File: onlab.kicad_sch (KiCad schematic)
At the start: 57 parts, among them J1 Battery, J2 HC_SR04, J3 HC_SR04, J4 HC_SR04, J5 DC-Motor, J6 DC-Motor, J7 DC-Motor, SW1 SW_SPDT, SW2 SW_SPDT, SW3 SW_DIP_x03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

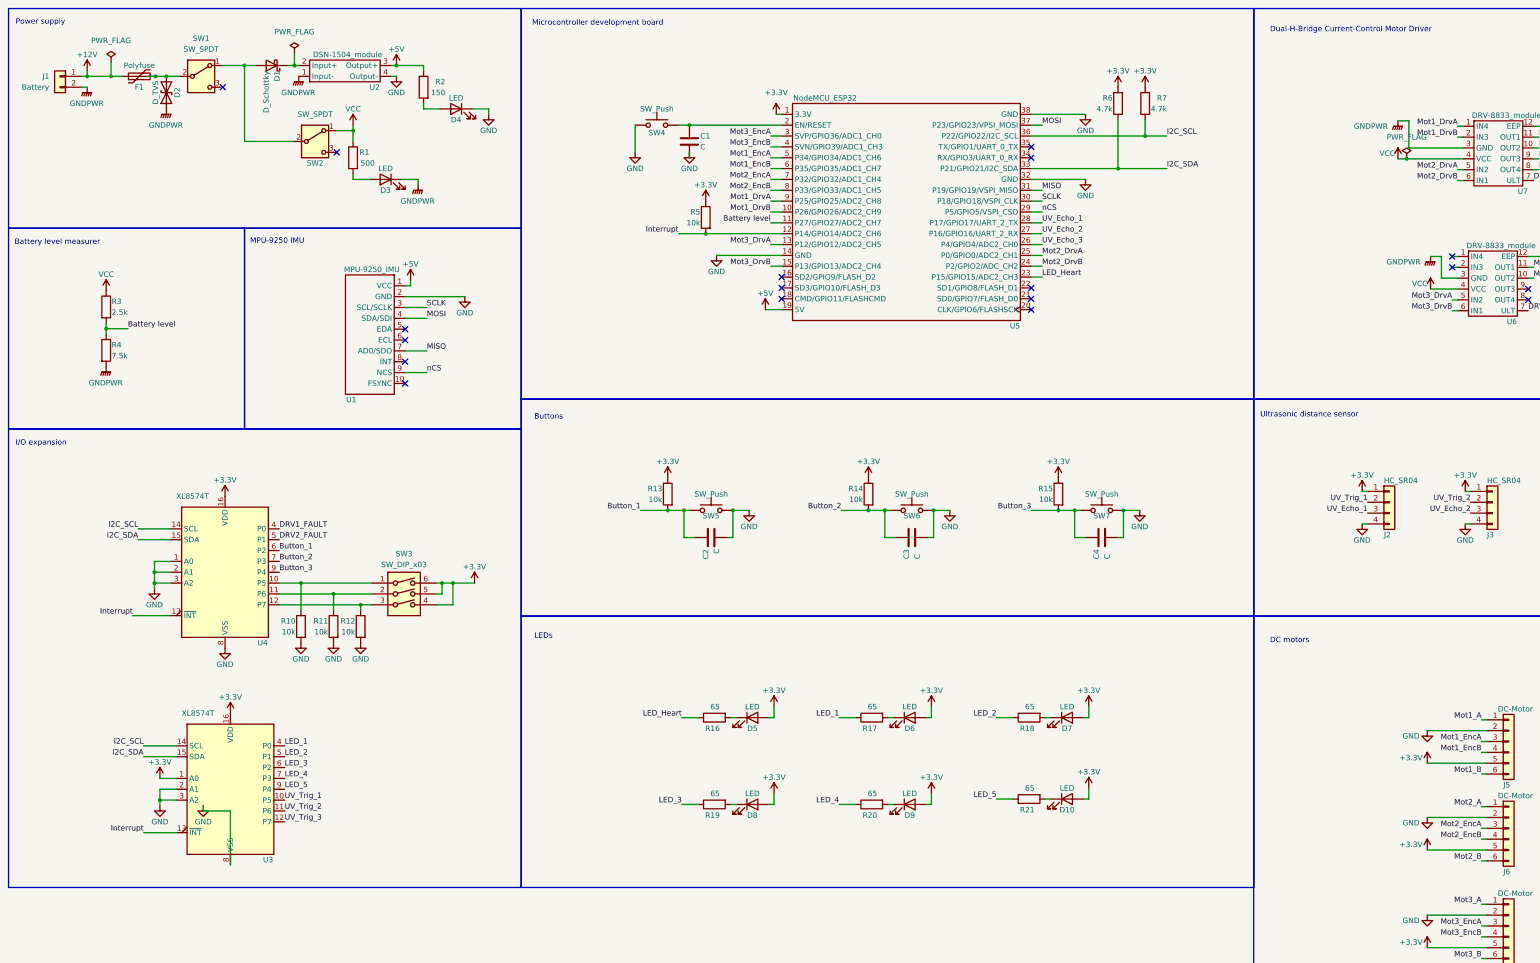
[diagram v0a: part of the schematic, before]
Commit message: Schematic and footprint update
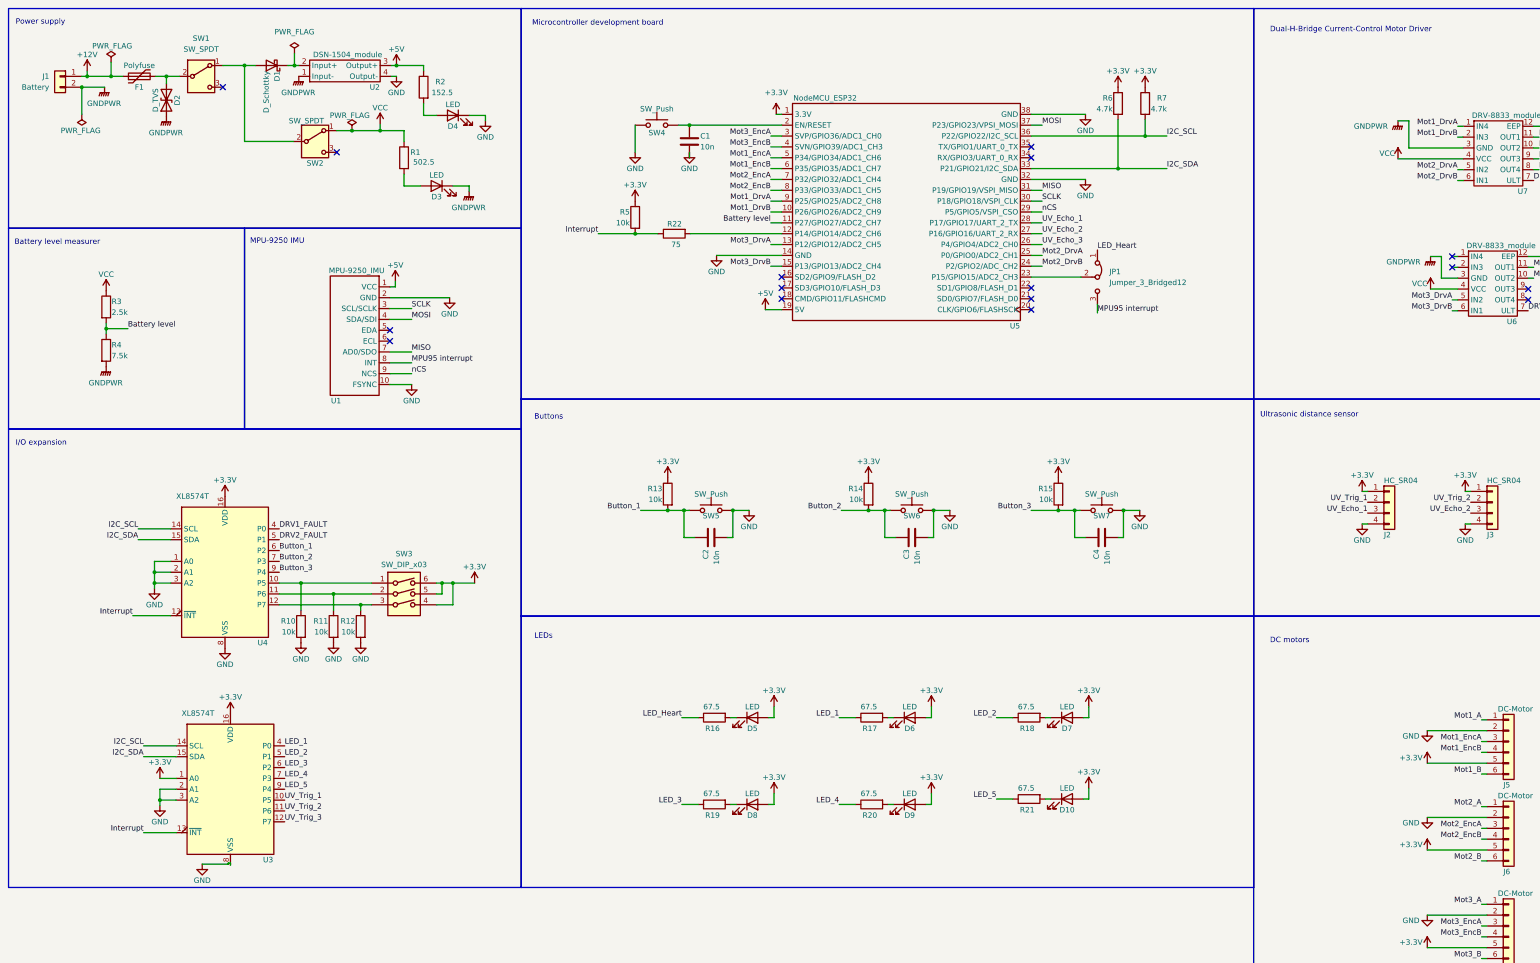
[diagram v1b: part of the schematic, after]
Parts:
- added JP1: Jumper_3_Bridged12, symbol Jumper:Jumper_3_Bridged12
- added R22: 75, Resistor_SMD:R_0805_2012Metric_Pad1.20x1.40mm_HandSolder, symbol Device:R
- C1, C2, C3, C4: value C -> 10n; footprint Capacitor_SMD:C_0805_2012Metric -> Capacitor_SMD:C_0805_2012Metric_Pad1.18x1.45mm_HandSolder
- D1: footprint (none) -> Diode_SMD:D_0805_2012Metric_Pad1.15x1.40mm_HandSolder
- D10, D3, D4, D5, D6, D7, D8, D9: footprint LED_SMD:LED_Kingbright_APHBM2012_2x1.25mm -> LED_SMD:LED_0805_2012Metric_Pad1.15x1.40mm_HandSolder
- D2: footprint (none) -> Diode_SMD:D_SMA_Handsoldering
- R1: value 500 -> 502.5; footprint (none) -> Resistor_SMD:R_0805_2012Metric_Pad1.20x1.40mm_HandSolder
- R10, R11, R12, R13, R14, R15, R3, R4, R5, R6, R7, R8, R9: footprint (none) -> Resistor_SMD:R_0805_2012Metric_Pad1.20x1.40mm_HandSolder
- R16, R17, R18, R19, R20, R21: value 65 -> 67.5; footprint (none) -> Resistor_SMD:R_0805_2012Metric_Pad1.20x1.40mm_HandSolder
- R2: value 150 -> 152.5; footprint (none) -> Resistor_SMD:R_0805_2012Metric_Pad1.20x1.40mm_HandSolder
- U2: footprint (none) -> Onlab:DSN1504_module
- U3, U4: footprint (none) -> Package_SO:SOIC-16W_7.5x10.3mm_P1.27mm
- U5: footprint (none) -> NodeMCU_ESP32:MODULE_NODEMCU-32S
- U6, U7: footprint (none) -> Onlab:DRV-8833_module
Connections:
- net GND: now also U1.10 (FSYNC)
- net Interrupt: now also R22.1; no longer U5.12 (P14/GPIO14/ADC2_CH6)
- net LED_Heart: now also JP1.1 (A); no longer U5.23 (P15/GPIO15/ADC2_CH3)
- net MPU95 interrupt: now reaches U1.8 (INT)
- net MPU95 interrupt: now also JP1.3 (B)
- new net: R22.2, U5.12 (P14/GPIO14/ADC2_CH6)
- new net: JP1.2 (C), U5.23 (P15/GPIO15/ADC2_CH3)
- no-connect marks 18 -> 16
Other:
- moved on the sheet: D2, D3, D4, R1, R5, U1

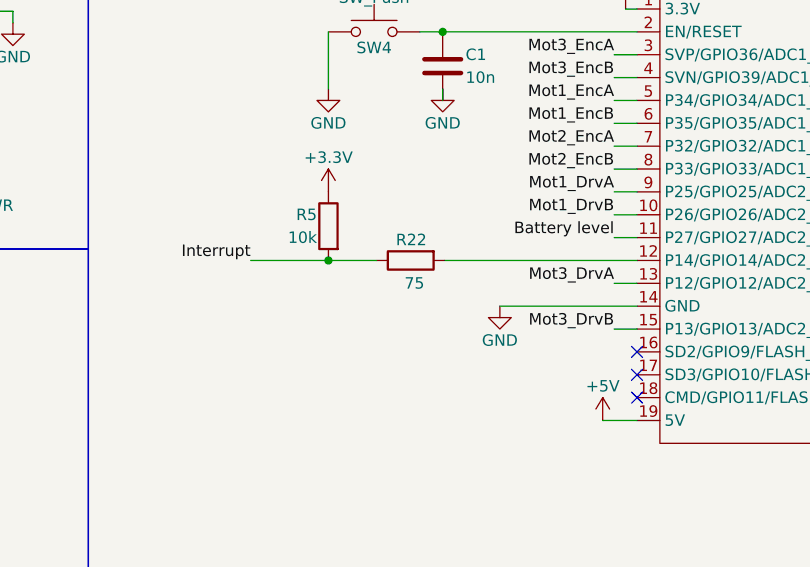
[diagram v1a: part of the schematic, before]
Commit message: resistor value
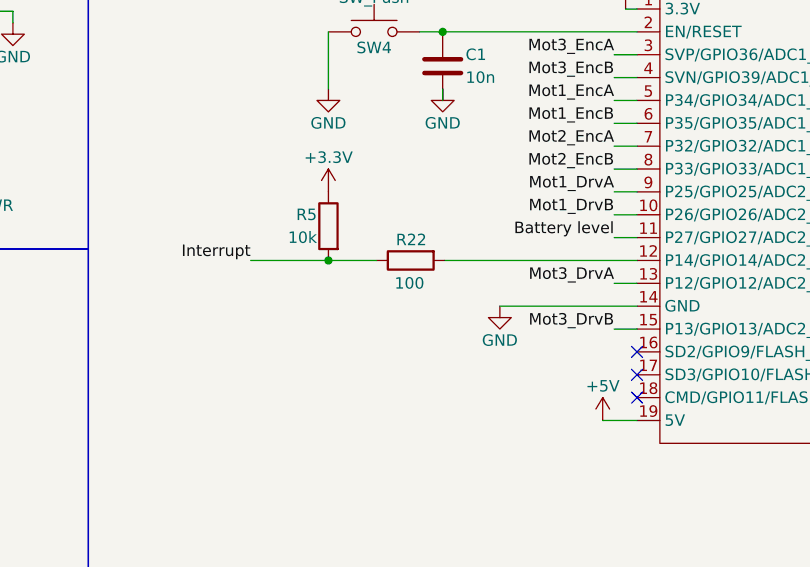
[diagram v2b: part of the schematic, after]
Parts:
- R22: value 75 -> 100
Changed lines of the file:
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@@
       (effects (font (size 1.27 1.27)) (justify left))
     )
-    (property "Value" "75" (at 169.418 67.31 90)
+    (property "Value" "100" (at 169.418 67.31 90)
       (effects (font (size 1.27 1.27)) (justify left))
     )

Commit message: schematic update
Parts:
- added Q1, Q2, Q3: NMOS, symbol Simulation_SPICE:NMOS
- added R23, R29, R33: 1k, Resistor_SMD:R_0805_2012Metric_Pad1.20x1.40mm_HandSolder, symbol Device:R
- added R24, R25, R26, R27, R28, R30, R31, R32, R34: 2k, Resistor_SMD:R_0805_2012Metric_Pad1.20x1.40mm_HandSolder, symbol Device:R
- F1: footprint (none) -> Fuse:Fuse_0805_2012Metric_Pad1.15x1.40mm_HandSolder
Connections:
- net +3.3V: now also Q1.2 (G), Q2.2 (G), Q3.2 (G), R25.1, R27.1, R31.1; no longer J2.1 (Pin_1), J3.1 (Pin_1), J4.1 (Pin_1)
- net +5V: now also J2.1 (Pin_1), J3.1 (Pin_1), J4.1 (Pin_1), R26.1, R30.1, R34.1
- net GND: now also R24.2, R28.2, R32.2
- net UV_Echo_1: now also R23.1, R24.1; no longer J2.3 (Pin_3)
- net UV_Echo_2: now also R28.1, R29.1; no longer J3.3 (Pin_3)
- net UV_Echo_3: now also R32.1, R33.1; no longer J4.3 (Pin_3)
- net UV_Trig_1: now also Q1.3 (S), R25.2; no longer J2.2 (Pin_2)
- net UV_Trig_2: now also Q2.3 (S), R27.2; no longer J3.2 (Pin_2)
- net UV_Trig_3: now also Q3.3 (S), R31.2; no longer J4.2 (Pin_2)
- new net: J4.3 (Pin_3), R33.2
- new net: J2.3 (Pin_3), R23.2
- new net: J3.2 (Pin_2), Q2.1 (D), R30.2
- new net: J4.2 (Pin_2), Q3.1 (D), R34.2
- new net: J2.2 (Pin_2), Q1.1 (D), R26.2
- new net: J3.3 (Pin_3), R29.2
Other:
- moved on the sheet: J2, J3, J4, J5, J6, J7

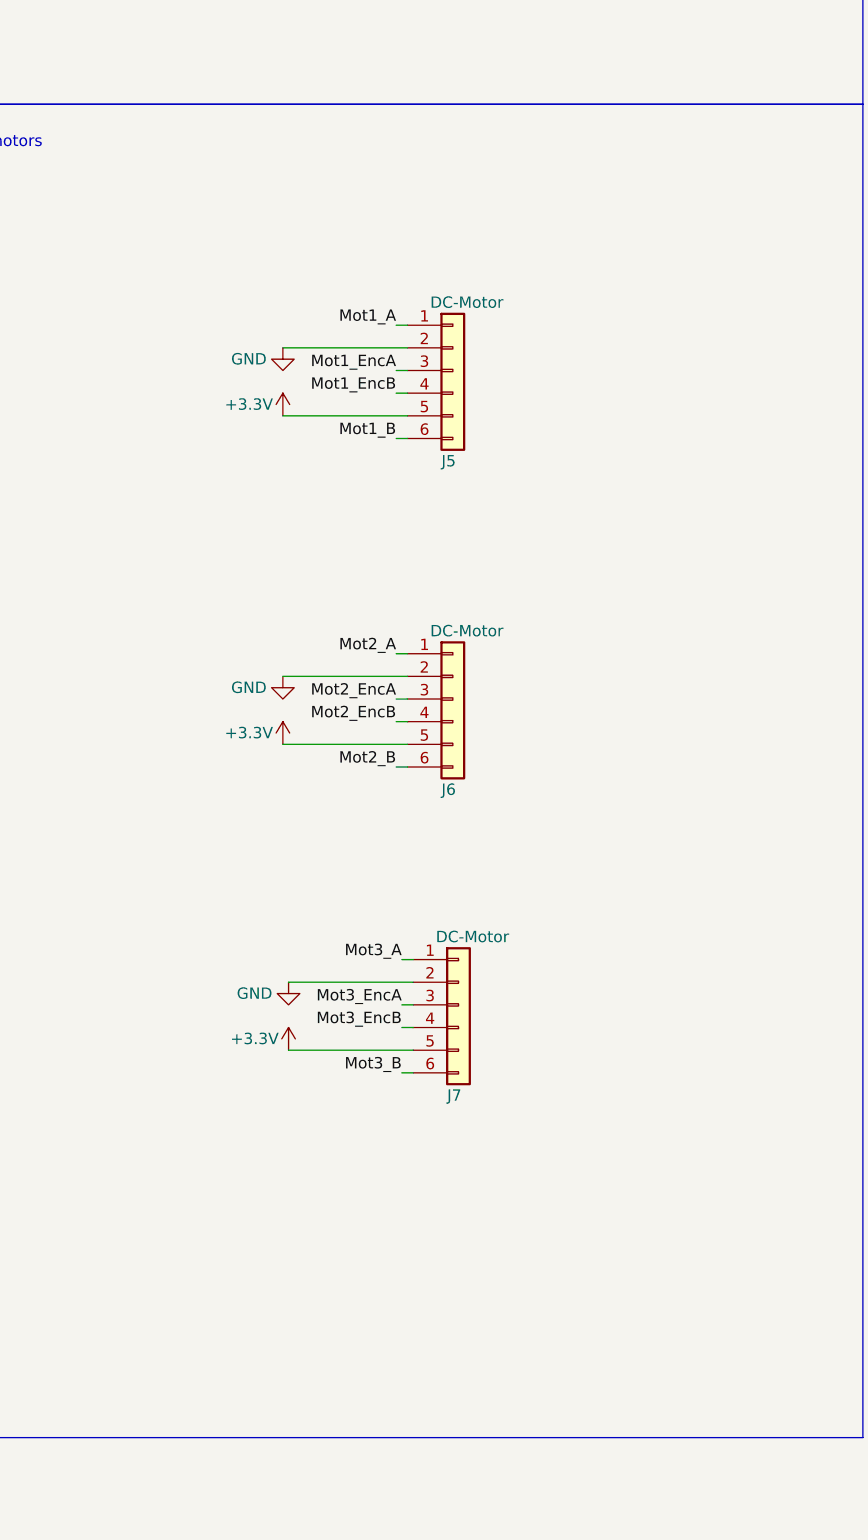
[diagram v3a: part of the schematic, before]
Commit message: schematic update: dc motor connectors
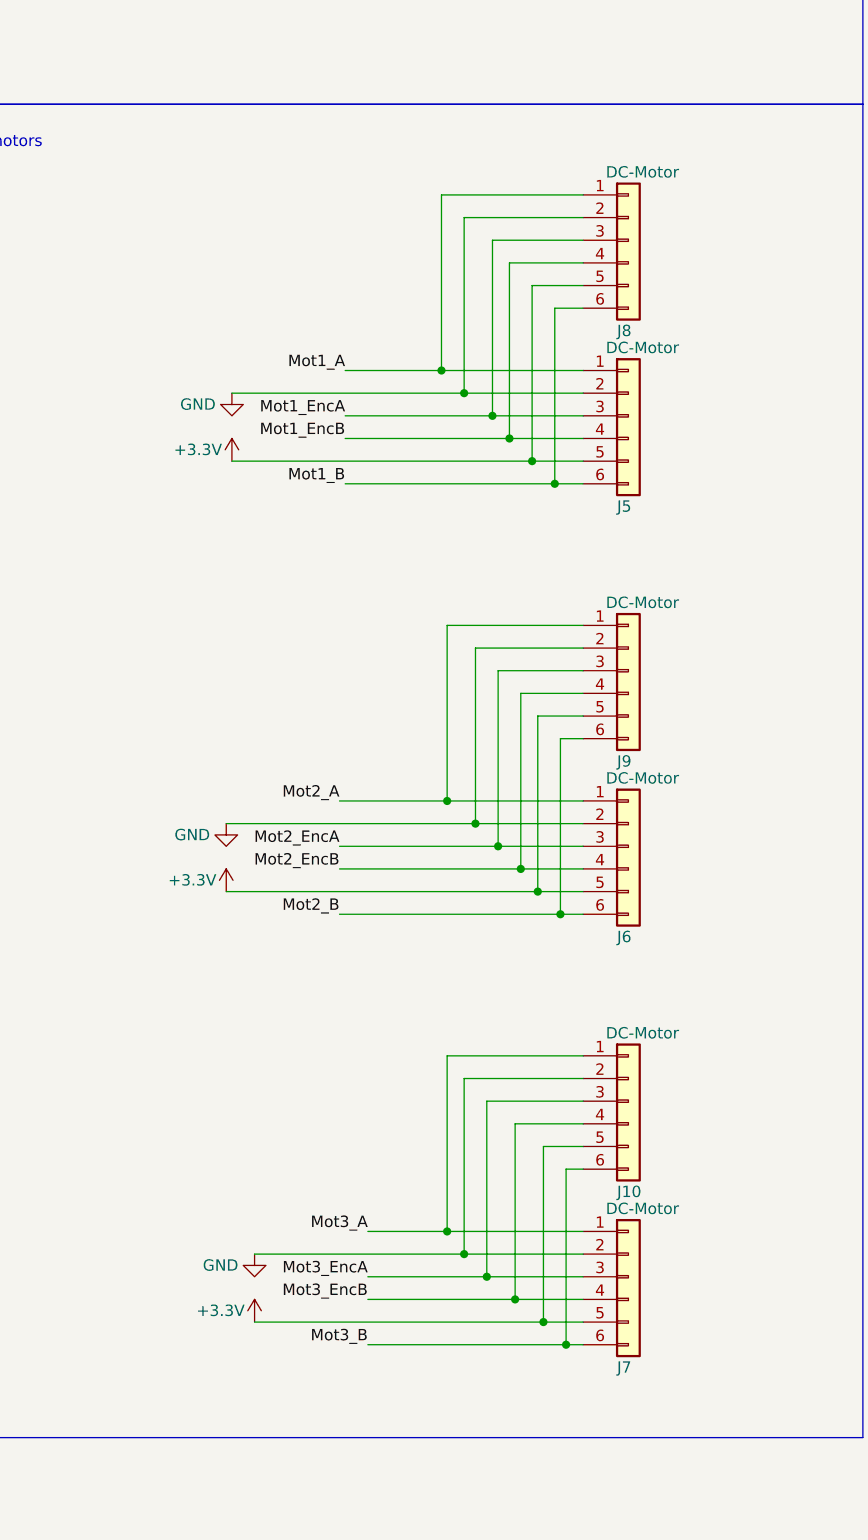
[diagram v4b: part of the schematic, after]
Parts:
- added J10, J8, J9: DC-Motor, Connector_Molex:Molex_KK-254_AE-6410-06A_1x06_P2.54mm_Vertical, symbol Connector_Generic:Conn_01x06
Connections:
- net +3.3V: now also J10.5 (Pin_5), J8.5 (Pin_5), J9.5 (Pin_5)
- net GND: now also J10.2 (Pin_2), J8.2 (Pin_2), J9.2 (Pin_2)
- net Mot1_A: now also J8.1 (Pin_1)
- net Mot1_B: now also J8.6 (Pin_6)
- net Mot1_EncA: now also J8.3 (Pin_3)
- net Mot1_EncB: now also J8.4 (Pin_4)
- net Mot2_A: now also J9.1 (Pin_1)
- net Mot2_B: now also J9.6 (Pin_6)
- net Mot2_EncA: now also J9.3 (Pin_3)
- net Mot2_EncB: now also J9.4 (Pin_4)
- net Mot3_A: now also J10.1 (Pin_1)
- net Mot3_B: now also J10.6 (Pin_6)
- net Mot3_EncA: now also J10.3 (Pin_3)
- net Mot3_EncB: now also J10.4 (Pin_4)
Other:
- moved on the sheet: J5, J6, J7
